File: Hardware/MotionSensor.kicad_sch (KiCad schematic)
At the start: 11 parts, among them U1 BNO085, Y1 Crystal_32.768kHz

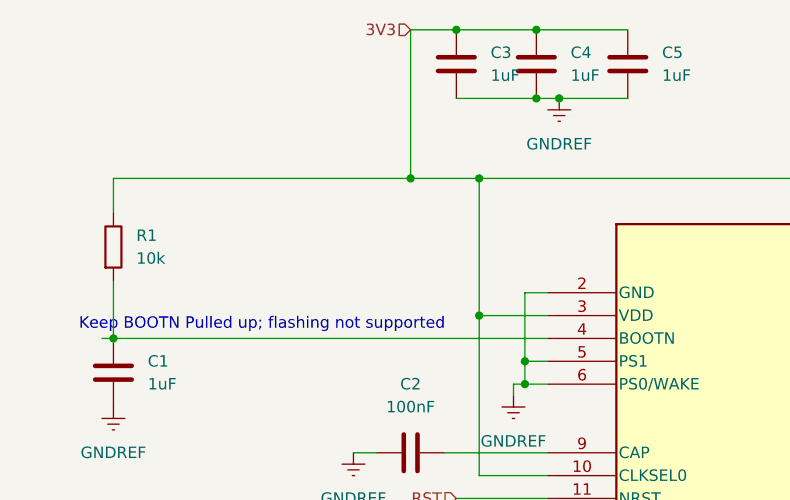
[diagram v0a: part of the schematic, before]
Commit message: Use tags for nets, apply netgroups, mess around in pcb view
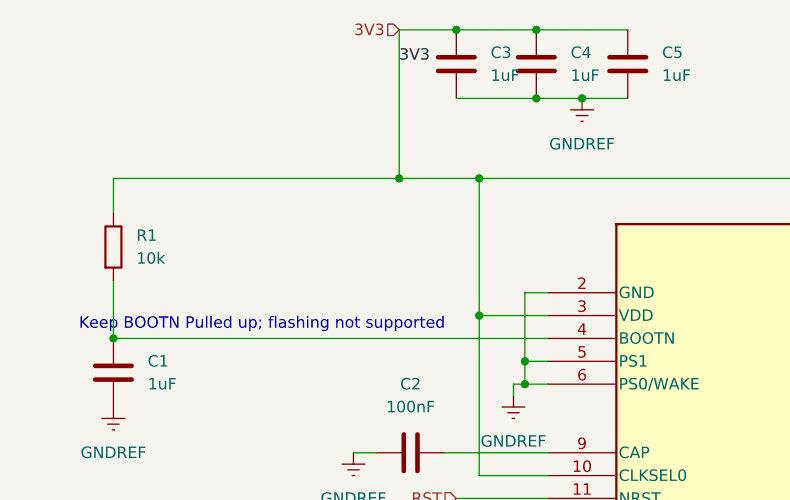
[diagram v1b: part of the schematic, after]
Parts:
- C1, C2, C3, C4, C5, C6, C7: footprint (none) -> Capacitor_SMD:C_0201_0603Metric
- R1: footprint Resistor_THT:R_Axial_DIN0207_L6.3mm_D2.5mm_P10.16mm_Horizontal -> Resistor_SMD:R_0201_0603Metric
- R2: footprint Resistor_THT:R_Axial_DIN0207_L6.3mm_D2.5mm_P10.16mm_Horizontal -> Resistor_SMD:R_0402_1005Metric
- U1: footprint LGA28_5.2X3.8_CEV -> Snapeda:LGA28_5.2X3.8_CEV
- Y1: footprint Crystal:Crystal_AT310_D3.0mm_L10.0mm_Horizontal -> Crystal:Crystal_SMD_3215-2Pin_3.2x1.5mm
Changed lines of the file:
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@@
-	)
-	(junction
-		(at 104.14 57.15)
-		(diameter 0)
-		(color 0 0 0 0)
 	)
 	(junction
@@
 	)
 	(junction
-		(at 87.63 66.04)
+		(at 86.36 66.04)
 		(diameter 0)
 		(color 0 0 0 0)
@@
 	)
 	(junction
+		(at 106.68 57.15)
+		(diameter 0)
+		(color 0 0 0 0)
+	)
+	(junction
 		(at 100.33 86.36)
 		(diameter 0)
@@
 	(wire
 		(pts
-			(xy 104.14 57.15) (xy 111.76 57.15)
-		)
-		(stroke
-			(width 0)
-			(type default)
-		)
-	)
-	(wire
-		(pts
 			(xy 173.99 76.2) (xy 181.61 76.2)
 		)
@@
 	(wire
 		(pts
-			(xy 53.34 83.82) (xy 54.61 83.82)
-		)
-		(stroke
-			(width 0)
-			(type default)
-		)
-	)
-	(wire
-		(pts
 			(xy 176.53 106.68) (xy 196.85 106.68)
 		)
@@
 	(wire
 		(pts
-			(xy 87.63 49.53) (xy 92.71 49.53)
-		)
-		(stroke
-			(width 0)
-			(type default)
-		)
-	)
-	(wire
-		(pts
-			(xy 87.63 66.04) (xy 95.25 66.04)
+			(xy 86.36 49.53) (xy 92.71 49.53)
 		)
 		(stroke
@@
 	(wire
 		(pts
-			(xy 54.61 66.04) (xy 87.63 66.04)
+			(xy 54.61 66.04) (xy 86.36 66.04)
 		)
 		(stroke
@@
 	(wire
 		(pts
+			(xy 86.36 66.04) (xy 95.25 66.04)
+		)
+		(stroke
+			(width 0)
+			(type default)
+		)
+	)
+	(wire
+		(pts
 			(xy 176.53 109.22) (xy 176.53 106.68)
 		)
@@
 	(wire
 		(pts
-			(xy 101.6 57.15) (xy 104.14 57.15)
+			(xy 101.6 57.15) (xy 106.68 57.15)
 		)
 		(stroke
@@
 	(wire
 		(pts
-			(xy 87.63 49.53) (xy 87.63 66.04)
+			(xy 86.36 49.53) (xy 86.36 66.04)
 		)
 		(stroke
@@
 		(pts
 			(xy 54.61 77.47) (xy 54.61 83.82)
+		)
+		(stroke
+			(width 0)
+			(type default)
+		)
+	)
+	(wire
+		(pts
+			(xy 106.68 57.15) (xy 111.76 57.15)
 		)
 		(stroke
@@
 		)
 	)
+	(label "3V3"
+		(at 86.36 53.34 0)
+		(fields_autoplaced yes)
+		(effects
+			(font
+				(size 1.27 1.27)
+			)
+			(justify left bottom)
+		)
+	)
 	(hierarchical_label "3V3"
 		(shape input)
-		(at 87.63 49.53 180)
+		(at 86.36 49.53 180)
 		(fields_autoplaced yes)
 		(effects
@@
 			)
 		)
-		(property "Footprint" "LGA28_5.2X3.8_CEV"
+		(property "Footprint" "Snapeda:LGA28_5.2X3.8_CEV"
 			(at 119.126 67.31 0)
 			(effects
@@
 			)
 		)
-		(property "Footprint" ""
+		(property "Footprint" "Capacitor_SMD:C_0201_0603Metric"
 			(at 102.5652 57.15 0)
 			(effects
@@
 			)
 		)
-		(property "Footprint" ""
+		(property "Footprint" "Capacitor_SMD:C_0201_0603Metric"
 			(at 93.6752 57.15 0)
 			(effects
@@
 			)
 		)
-		(property "Footprint" ""
+		(property "Footprint" "Capacitor_SMD:C_0201_0603Metric"
 			(at 91.44 95.5548 0)
 			(effects
@@
 			)
 		)
-		(property "Footprint" ""
+		(property "Footprint" "Capacitor_SMD:C_0201_0603Metric"
 			(at 232.1052 90.17 0)
 			(effects
@@
 			)
 		)
-		(property "Footprint" ""
+		(property "Footprint" "Capacitor_SMD:C_0201_0603Metric"
 			(at 112.7252 57.15 0)
 			(effects
@@
 			)
 		)
-		(property "Footprint" ""
+		(property "Footprint" "Capacitor_SMD:C_0201_0603Metric"
 			(at 214.3252 90.17 0)
 			(effects
@@
 			)
 		)
-		(property "Footprint" "Resistor_THT:R_Axial_DIN0207_L6.3mm_D2.5mm_P10.16mm_Horizontal"
+		(property "Footprint" "Resistor_SMD:R_0201_0603Metric"
 			(at 58.928 72.771 0)
 			(effects
@@
 			)
 		)
-		(property "Footprint" ""
+		(property "Footprint" "Capacitor_SMD:C_0201_0603Metric"
 			(at 55.5752 91.44 0)
 			(effects
@@
 			)
 		)
-		(property "Footprint" "Crystal:Crystal_AT310_D3.0mm_L10.0mm_Horizontal"
+		(property "Footprint" "Crystal:Crystal_SMD_3215-2Pin_3.2x1.5mm"
 			(at 222.25 81.28 0)
 			(effects
@@
 	(symbol
 		(lib_id "PartsLib:GNDREF")
-		(at 104.14 57.15 0)
+		(at 106.68 57.15 0)
 		(unit 1)
 		(exclude_from_sim no)
@@
 		(fields_autoplaced yes)
 		(property "Reference" "#PWR04"
-			(at 104.14 63.5 0)
+			(at 106.68 63.5 0)
 			(effects
 				(font
@@
 		)
 		(property "Value" "GNDREF"
-			(at 104.14 62.23 0)
+			(at 106.68 62.23 0)
 			(effects
 				(font
@@
 		)
 		(property "Footprint" ""
-			(at 104.14 57.15 0)
+			(at 106.68 57.15 0)
 			(effects
 				(font
@@
 		)
 		(property "Datasheet" ""
-			(at 104.14 57.15 0)
+			(at 106.68 57.15 0)
 			(effects
 				(font
@@
 		)
 		(property "Description" "Power symbol creates a global label with name \"GNDREF\" , reference supply ground"
-			(at 104.14 57.15 0)
+			(at 106.68 57.15 0)
 			(effects
 				(font
@@
 			)
 		)
-		(property "Footprint" "Resistor_THT:R_Axial_DIN0207_L6.3mm_D2.5mm_P10.16mm_Horizontal"
+		(property "Footprint" "Resistor_SMD:R_0402_1005Metric"
 			(at 192.532 103.759 0)
 			(effects

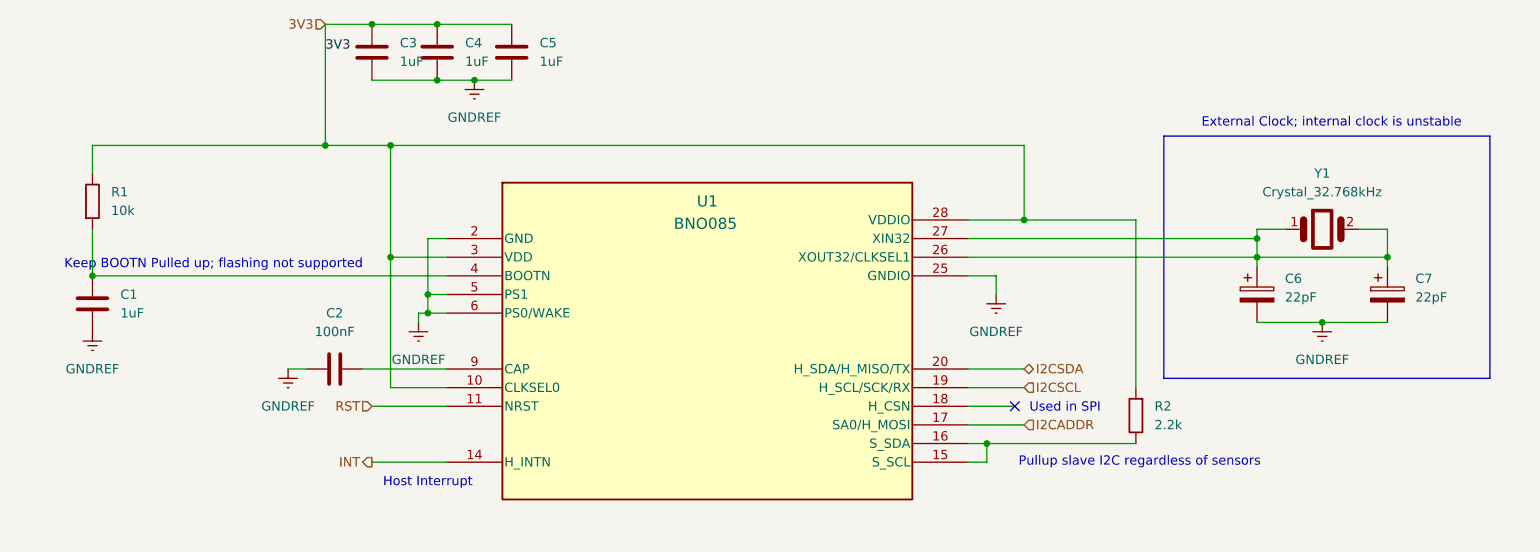
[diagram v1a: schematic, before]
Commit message: Use Peanut symbols, fix ERC errors, progress on DAC & Pressure
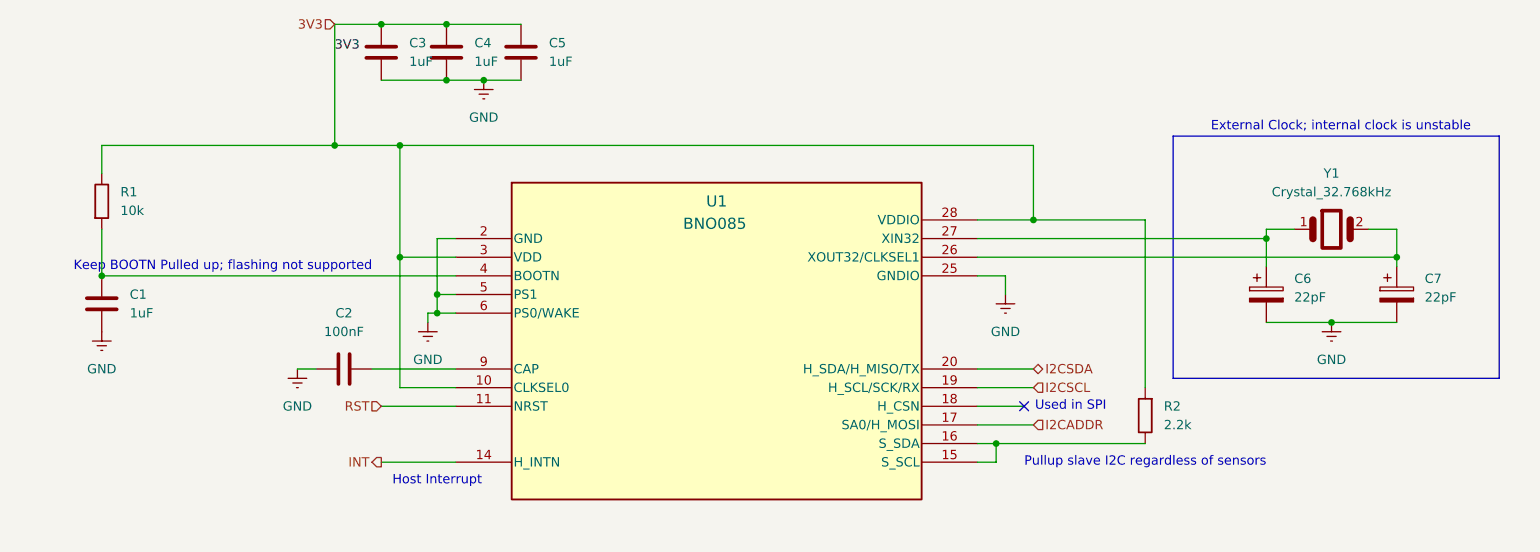
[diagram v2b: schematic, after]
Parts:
- removed Y1: Crystal_32.768kHz, Crystal:Crystal_SMD_3215-2Pin_3.2x1.5mm, symbol PCM_SL_Devices:Crystal_32.768kHz
- added Y1: Crystal_32.768kHz, Crystal:Crystal_SMD_3215-2Pin_3.2x1.5mm, symbol Peanut:Crystal_32.768kHz
- R1: symbol PCM_SL_Resistors:10k -> Peanut:R
- R2: footprint Resistor_SMD:R_0402_1005Metric -> Resistor_SMD:R_0201_0603Metric; symbol PCM_SL_Resistors:2.2k -> Peanut:R
- U1: footprint Snapeda:LGA28_5.2X3.8_CEV -> Peanut:LGA28_5.2X3.8_CEV; Manufacturer (none) -> CEVA
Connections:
- net at C7.1, U1.26 (XOUT32/CLKSEL1): now also Y1.2; no longer C6.1, U1.27 (XIN32)
- net GNDREF renamed GND
- new net: C6.1, U1.27 (XIN32), Y1.1
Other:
- moved on the sheet: C1, C2, C3, C4, C5, C6, C7, R1, R2, U1

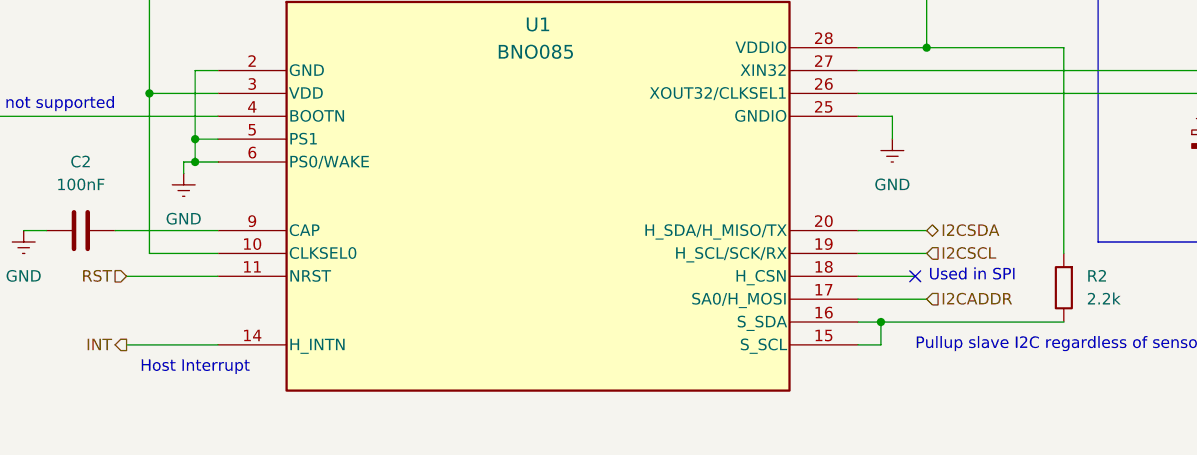
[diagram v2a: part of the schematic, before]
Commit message: Add Battery Monitoring & Use Project Parts Library
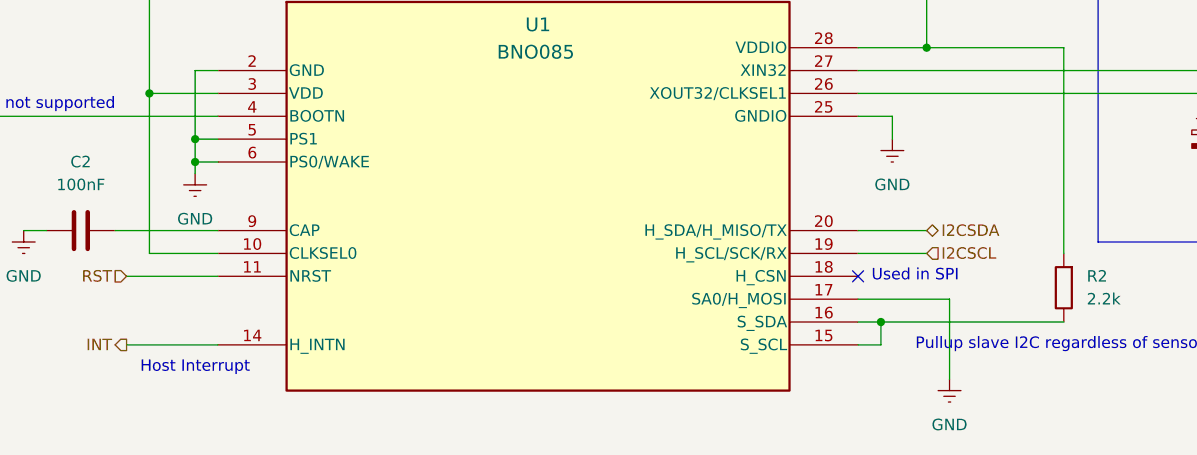
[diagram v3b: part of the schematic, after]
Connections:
- net I2CADDR is gone; now on net GND: U1.17 (SA0/H_MOSI)
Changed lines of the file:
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@@
 	)
 	(no_connect
-		(at 181.61 101.6)
+		(at 175.26 101.6)
 	)
 	(wire
@@
 	(wire
 		(pts
+			(xy 175.26 104.14) (xy 185.42 104.14)
+		)
+		(stroke
+			(width 0)
+			(type default)
+		)
+	)
+	(wire
+		(pts
 			(xy 177.8 106.68) (xy 198.12 106.68)
 		)
@@
 	(wire
 		(pts
+			(xy 185.42 104.14) (xy 185.42 113.03)
+		)
+		(stroke
+			(width 0)
+			(type default)
+		)
+	)
+	(wire
+		(pts
 			(xy 175.26 109.22) (xy 177.8 109.22)
 		)
@@
 	(wire
 		(pts
-			(xy 175.26 101.6) (xy 181.61 101.6)
-		)
-		(stroke
-			(width 0)
-			(type default)
-		)
-	)
-	(wire
-		(pts
-			(xy 100.33 88.9) (xy 101.6 88.9)
-		)
-		(stroke
-			(width 0)
-			(type default)
-		)
-	)
-	(wire
-		(pts
 			(xy 101.6 88.9) (xy 104.14 88.9)
 		)
@@
 	(wire
 		(pts
-			(xy 100.33 88.9) (xy 100.33 90.17)
+			(xy 101.6 88.9) (xy 101.6 90.17)
 		)
 		(stroke
@@
 		(pts
 			(xy 182.88 76.2) (xy 198.12 76.2)
-		)
-		(stroke
-			(width 0)
-			(type default)
-		)
-	)
-	(wire
-		(pts
-			(xy 175.26 104.14) (xy 182.88 104.14)
 		)
 		(stroke
@@
 	(text "Used in SPI"
 		(exclude_from_sim no)
-		(at 187.96 101.6 0)
+		(at 181.61 101.6 0)
 		(effects
 			(font
@@
 		(shape input)
 		(at 182.88 99.06 0)
-		(fields_autoplaced yes)
-		(effects
-			(font
-				(size 1.27 1.27)
-			)
-			(justify left)
-		)
-	)
-	(hierarchical_label "I2CADDR"
-		(shape input)
-		(at 182.88 104.14 0)
 		(fields_autoplaced yes)
 		(effects
@@
 	)
 	(symbol
+		(lib_id "Peanut:GND")
+		(at 185.42 113.03 0)
+		(unit 1)
+		(exclude_from_sim no)
+		(in_bom yes)
+		(on_board yes)
+		(dnp no)
+		(fields_autoplaced yes)
+		(property "Reference" "#PWR038"
+			(at 185.42 119.38 0)
+			(effects
+				(font
+					(size 1.27 1.27)
+				)
+				(hide yes)
+			)
+		)
+		(property "Value" "GND"
+			(at 185.42 118.11 0)
+			(effects
+				(font
+					(size 1.27 1.27)
+				)
+			)
+		)
+		(property "Footprint" ""
+			(at 185.42 113.03 0)
+			(effects
+				(font
+					(size 1.27 1.27)
+				)
+				(hide yes)
+			)
+		)
+		(property "Datasheet" ""
+			(at 185.42 113.03 0)
+			(effects
+				(font
+					(size 1.27 1.27)
+				)
+				(hide yes)
+			)
+		)
+		(property "Description" ""
+			(at 185.42 121.666 0)
+			(effects
+				(font
+					(size 1.27 1.27)
+				)
+				(hide yes)
+			)
+		)
+		(pin "1"
+		)
+		(instances
+			(project "Peanut"
+				(path "/298ef215-2a76-4225-b9ba-26c57869f278/9f632c63-9e97-4340-a214-949adeb3cd46"
+					(reference "#PWR038")
+					(unit 1)
+				)
+			)
+		)
+	)
+	(symbol
 		(lib_id "Device:C")
 		(at 113.03 53.34 0)
@@
 			)
 		)
-		(property "Description" "2.2kΩ, 1/4W Resistor"
+		(property "Description" "Resistor"
 			(at 55.88 73.66 0)
 			(effects
@@
 	(symbol
 		(lib_id "Peanut:GND")
-		(at 100.33 90.17 0)
+		(at 101.6 90.17 0)
 		(unit 1)
 		(exclude_from_sim no)
@@
 		(fields_autoplaced yes)
 		(property "Reference" "#PWR03"
-			(at 100.33 96.52 0)
+			(at 101.6 96.52 0)
 			(effects
 				(font
@@
 		)
 		(property "Value" "GND"
-			(at 100.33 95.25 0)
+			(at 101.6 95.25 0)
 			(effects
 				(font
@@
 		)
 		(property "Footprint" ""
-			(at 100.33 90.17 0)
+			(at 101.6 90.17 0)
 			(effects
 				(font
@@
 		)
 		(property "Datasheet" ""
-			(at 100.33 90.17 0)
+			(at 101.6 90.17 0)
 			(effects
 				(font
@@
 		)
 		(property "Description" ""
-			(at 100.33 98.806 0)
+			(at 101.6 98.806 0)
 			(effects
 				(font
@@
 			)
 		)
-		(property "Description" "2.2kΩ, 1/4W Resistor"
+		(property "Description" "Resistor"
 			(at 198.12 102.87 0)
 			(effects

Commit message: Fully wired board!
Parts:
- C1, C2, C3, C4, C5: footprint Capacitor_SMD:C_0201_0603Metric -> Resistor_SMD:R_01005_0402Metric; symbol Device:C -> Peanut:C
- R1, R2: footprint Resistor_SMD:R_0201_0603Metric -> Resistor_SMD:R_0402_1005Metric
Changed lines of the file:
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@@
 	)
 	(symbol
-		(lib_id "Device:C")
+		(lib_id "Peanut:C")
 		(at 102.87 53.34 0)
 		(unit 1)
@@
 			)
 		)
-		(property "Footprint" "Capacitor_SMD:C_0201_0603Metric"
+		(property "Footprint" "Resistor_SMD:R_01005_0402Metric"
 			(at 103.8352 57.15 0)
 			(effects
@@
 	)
 	(symbol
-		(lib_id "Device:C")
+		(lib_id "Peanut:C")
 		(at 93.98 53.34 0)
 		(unit 1)
@@
 			)
 		)
-		(property "Footprint" "Capacitor_SMD:C_0201_0603Metric"
+		(property "Footprint" "Resistor_SMD:R_01005_0402Metric"
 			(at 94.9452 57.15 0)
 			(effects
@@
 	)
 	(symbol
-		(lib_id "Device:C")
+		(lib_id "Peanut:C")
 		(at 88.9 96.52 90)
 		(unit 1)
@@
 			)
 		)
-		(property "Footprint" "Capacitor_SMD:C_0201_0603Metric"
+		(property "Footprint" "Resistor_SMD:R_01005_0402Metric"
 			(at 92.71 95.5548 0)
 			(effects
@@
 	)
 	(symbol
-		(lib_id "Device:C")
+		(lib_id "Peanut:C")
 		(at 113.03 53.34 0)
 		(unit 1)
@@
 			)
 		)
-		(property "Footprint" "Capacitor_SMD:C_0201_0603Metric"
+		(property "Footprint" "Resistor_SMD:R_01005_0402Metric"
 			(at 113.9952 57.15 0)
 			(effects
@@
 			)
 		)
-		(property "Footprint" "Resistor_SMD:R_0201_0603Metric"
+		(property "Footprint" "Resistor_SMD:R_0402_1005Metric"
 			(at 60.198 72.771 0)
 			(effects
@@
 	)
 	(symbol
-		(lib_id "Device:C")
+		(lib_id "Peanut:C")
 		(at 55.88 87.63 0)
 		(unit 1)
@@
 			)
 		)
-		(property "Footprint" "Capacitor_SMD:C_0201_0603Metric"
+		(property "Footprint" "Resistor_SMD:R_01005_0402Metric"
 			(at 56.8452 91.44 0)
 			(effects
@@
 			)
 		)
-		(property "Footprint" "Resistor_SMD:R_0201_0603Metric"
+		(property "Footprint" "Resistor_SMD:R_0402_1005Metric"
 			(at 193.802 103.759 0)
 			(effects

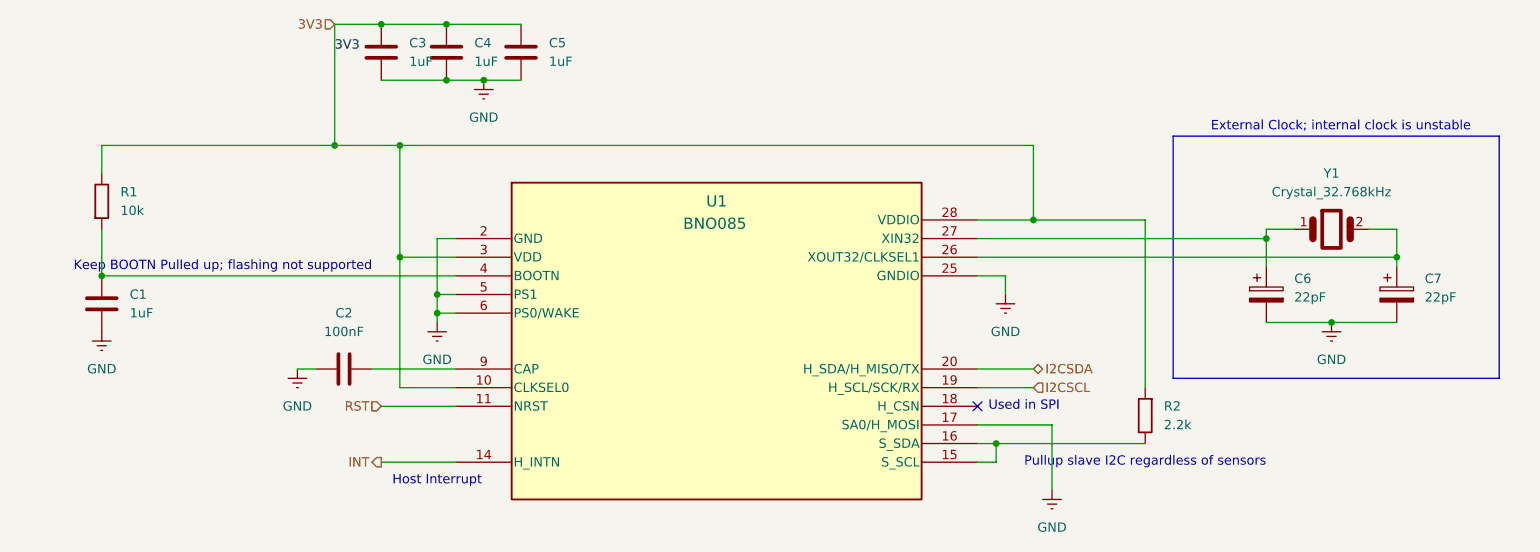
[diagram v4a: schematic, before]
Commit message: Initial OS architecture, and updated PCB work After a joint planning session, designed and architected OS structure: ``` src/ |- os: Audio, Accelerometer, Humidity, etc |- drivers: I2C interfaces, per-chip ```
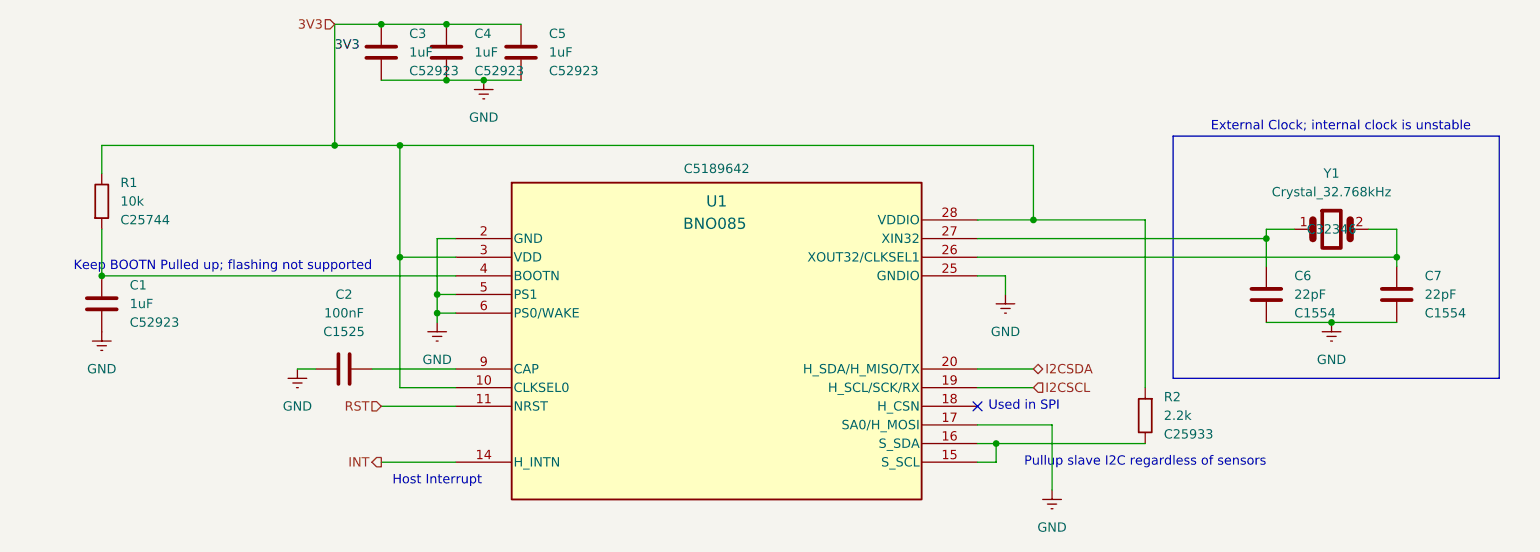
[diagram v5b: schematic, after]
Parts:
- C1, C3, C4, C5: footprint Resistor_SMD:R_01005_0402Metric -> Capacitor_SMD:C_0402_1005Metric; symbol Peanut:C -> Peanut:C 1uF; LCSC (none) -> C52923
- C2: footprint Resistor_SMD:R_01005_0402Metric -> Capacitor_SMD:C_0402_1005Metric; symbol Peanut:C -> Peanut:C 100nF; LCSC (none) -> C1525
- C6, C7: footprint Capacitor_SMD:C_0201_0603Metric -> Capacitor_SMD:C_0402_1005Metric; symbol Device:C_Polarized -> Peanut:C 22pF; LCSC (none) -> C1554
- R1: symbol Peanut:R -> Peanut:R 10k; LCSC (none) -> C25744
- R2: symbol Peanut:R -> Peanut:R 2.2k; LCSC (none) -> C25933
- U1: LCSC (none) -> C5189642
- Y1: LCSC (none) -> C32346
